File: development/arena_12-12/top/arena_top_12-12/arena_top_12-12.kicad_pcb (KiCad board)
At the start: 6 copper layers, 228.6 x 228.6 mm, 29 parts, among them J4 Barrel_Jack, P1 CONN15, P10 CONN15, P11 CONN15, P12 CONN15, P2 CONN15, P3 CONN15, P4 CONN15, P5 CONN15, P6 CONN15, P7 CONN15, P8 CONN15, P9 CONN15

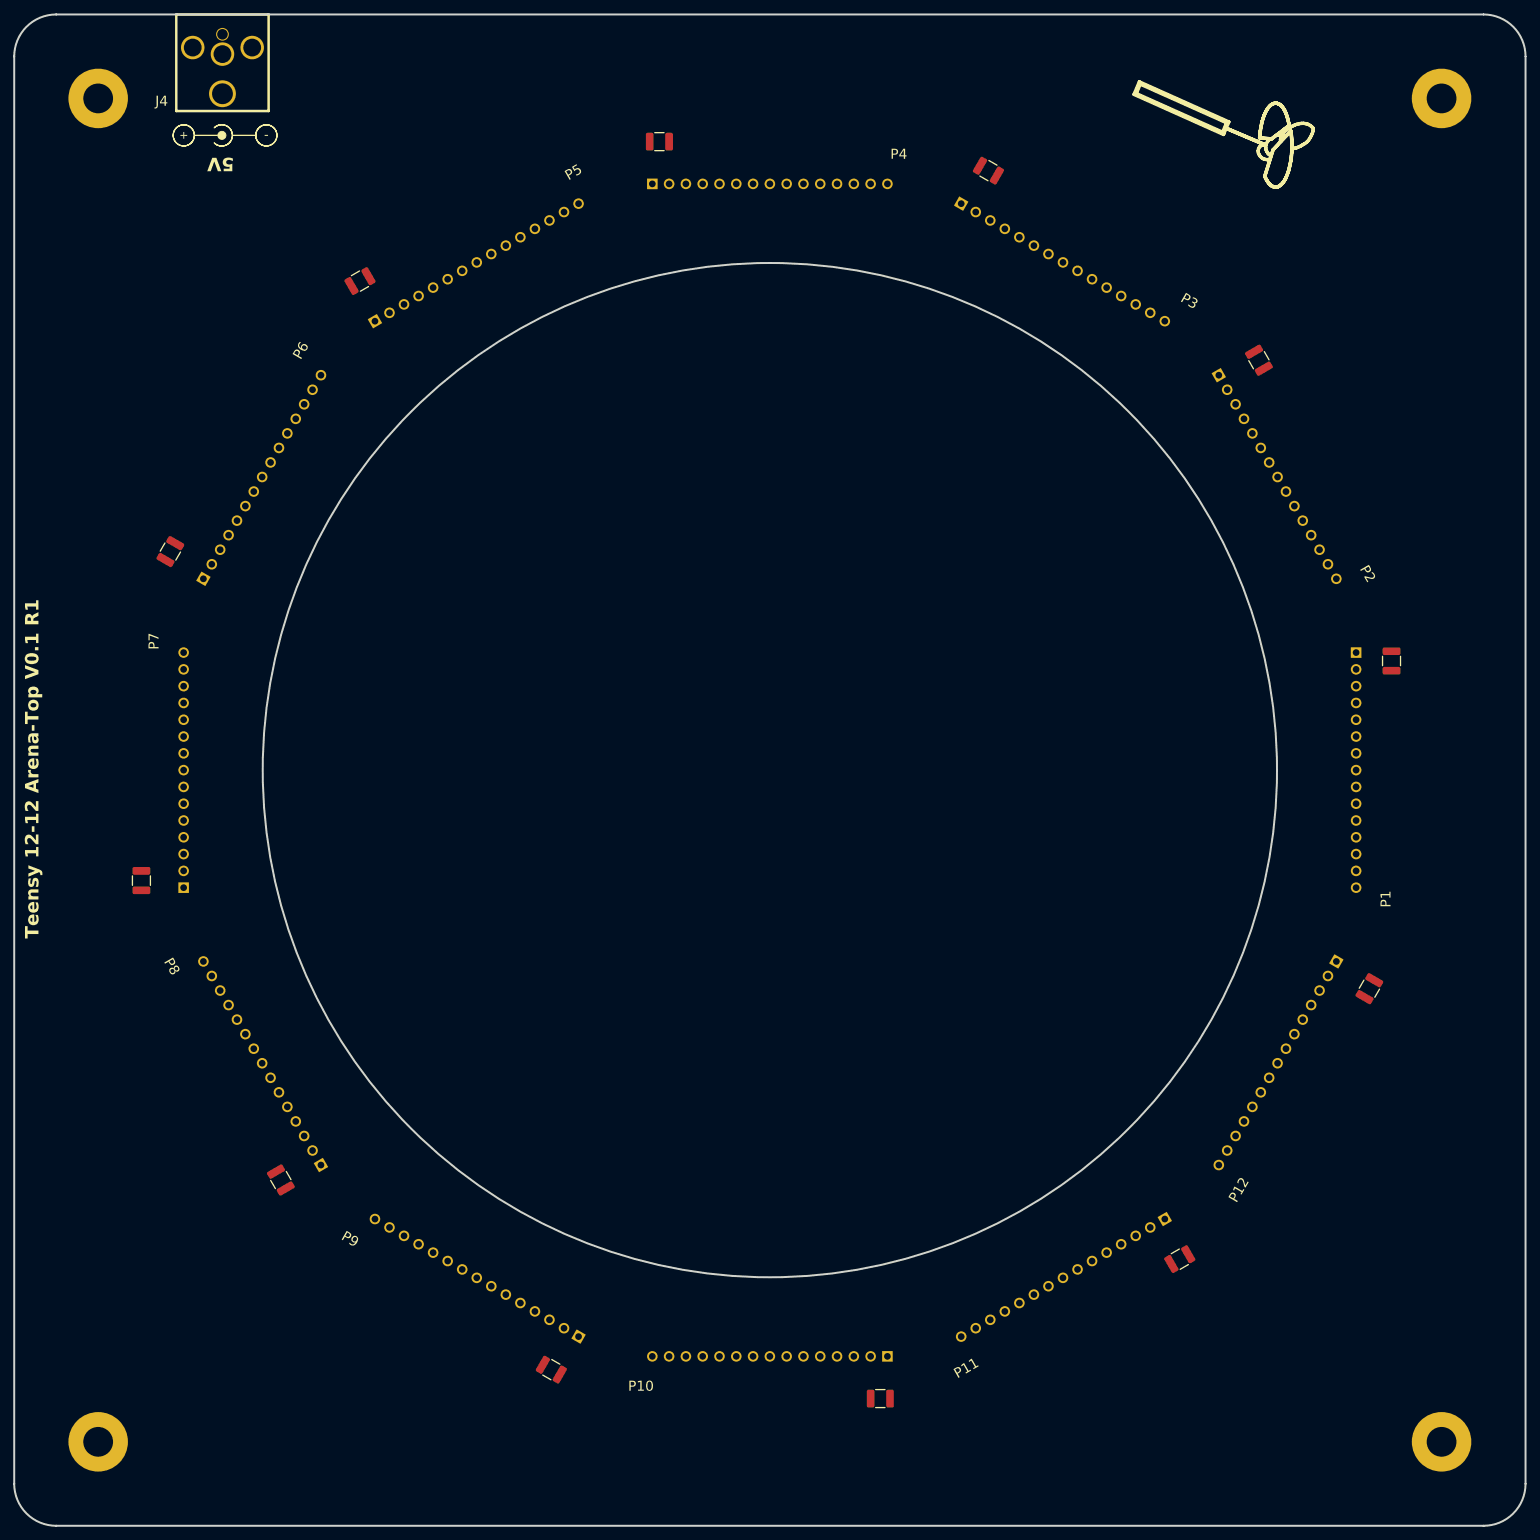
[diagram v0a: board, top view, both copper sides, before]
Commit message: Finished hand route of 12-12 teensy arena. Finished route of 12-12 top.
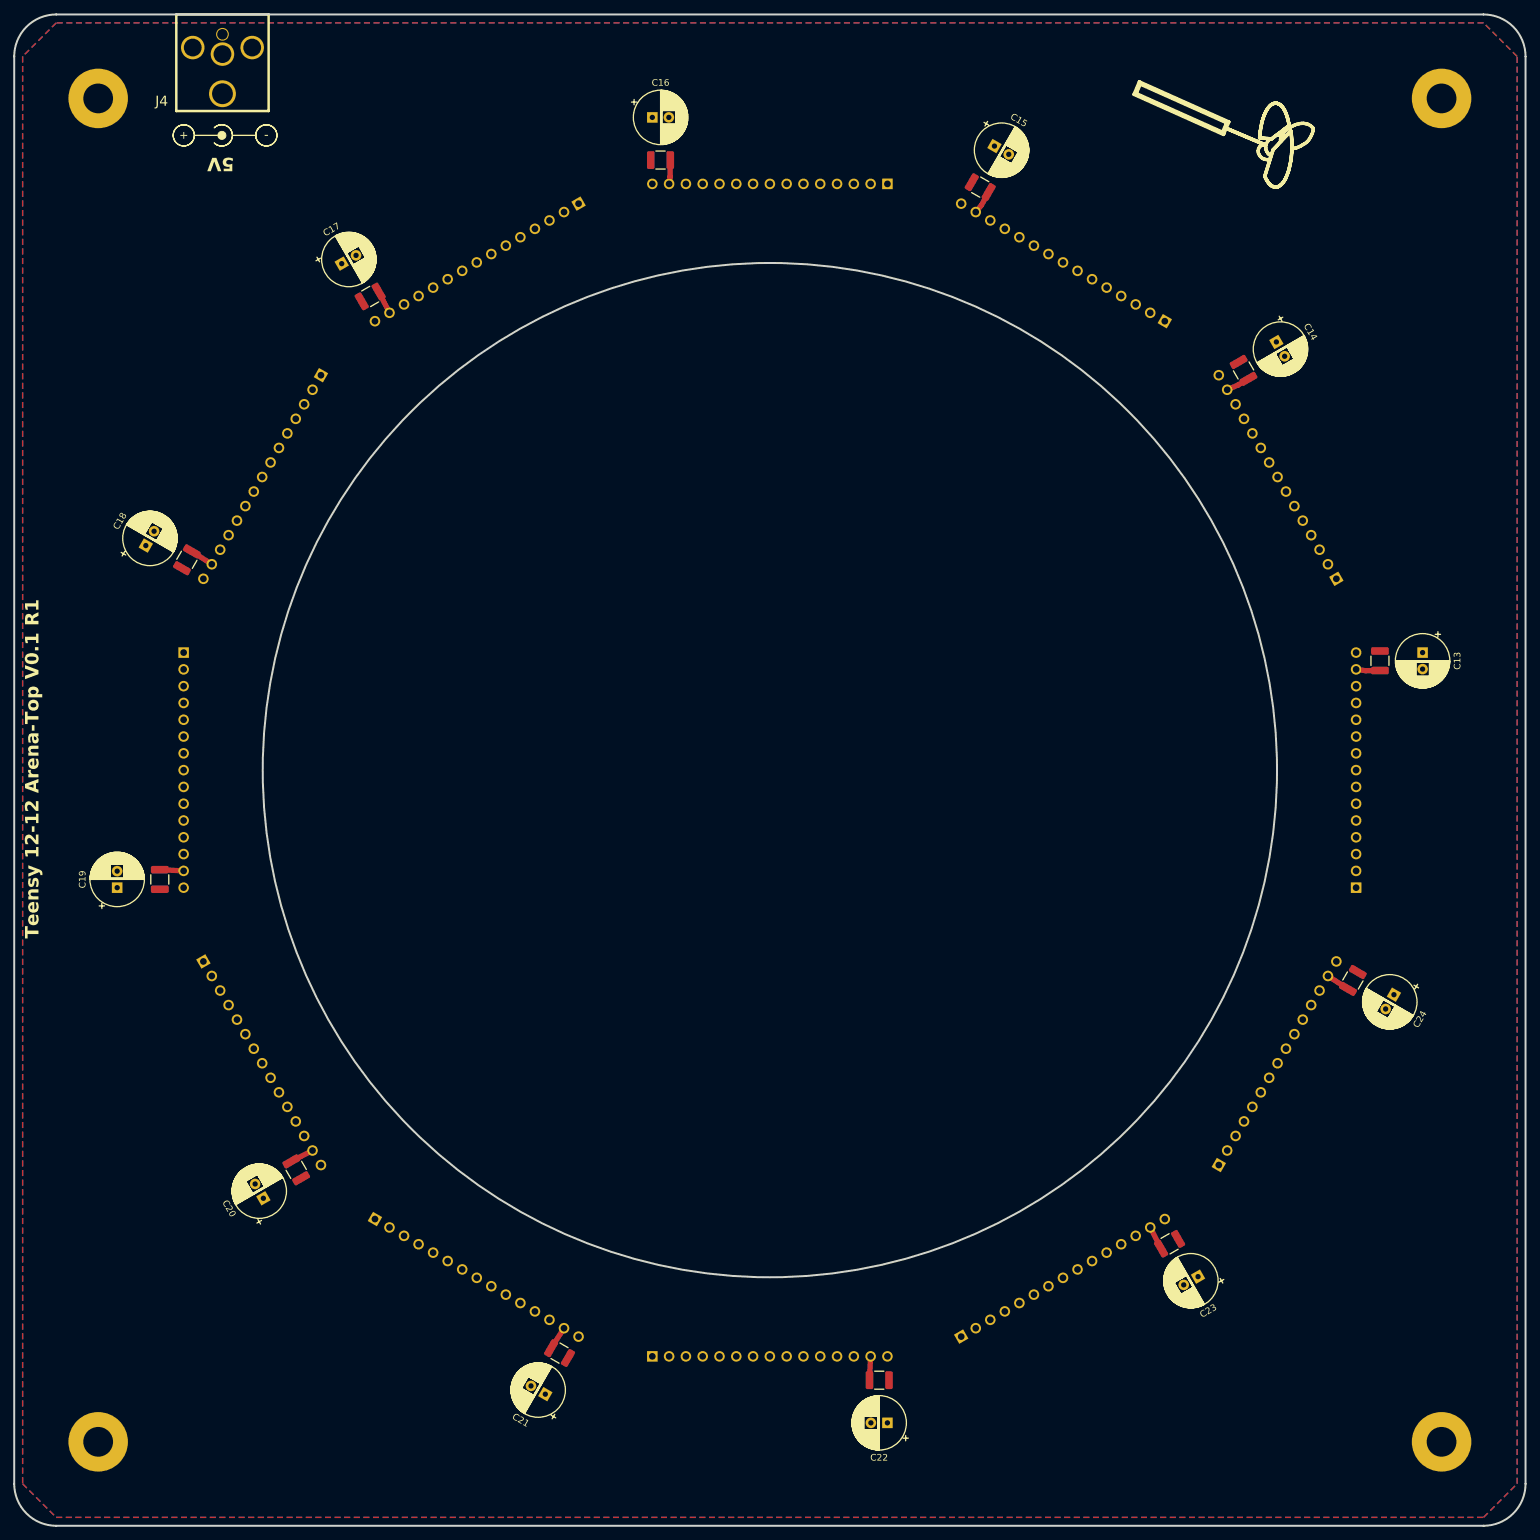
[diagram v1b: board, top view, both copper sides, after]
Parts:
- added C13: C_Polarized, Capacitor_THT:CP_Radial_D8.0mm_P2.50mm, F.Cu at (276.5, 160.0)
- added C14: C_Polarized, Capacitor_THT:CP_Radial_D8.0mm_P2.50mm, F.Cu at (254.4, 113.0)
- added C15: C_Polarized, Capacitor_THT:CP_Radial_D8.0mm_P2.50mm, F.Cu at (211.8, 83.4)
- added C16: C_Polarized, Capacitor_THT:CP_Radial_D8.0mm_P2.50mm, F.Cu at (160.0, 79.1)
- added C17: C_Polarized, Capacitor_THT:CP_Radial_D8.0mm_P2.50mm, F.Cu at (113.0, 101.2)
- added C18: C_Polarized, Capacitor_THT:CP_Radial_D8.0mm_P2.50mm, F.Cu at (83.4, 143.8)
- added C19: C_Polarized, Capacitor_THT:CP_Radial_D8.0mm_P2.50mm, F.Cu at (79.1, 195.6)
- added C20: C_Polarized, Capacitor_THT:CP_Radial_D8.0mm_P2.50mm, F.Cu at (101.2, 242.6)
- added C21: C_Polarized, Capacitor_THT:CP_Radial_D8.0mm_P2.50mm, F.Cu at (143.8, 272.2)
- added C22: C_Polarized, Capacitor_THT:CP_Radial_D8.0mm_P2.50mm, F.Cu at (195.6, 276.5)
- added C23: C_Polarized, Capacitor_THT:CP_Radial_D8.0mm_P2.50mm, F.Cu at (242.6, 254.4)
- added C24: C_Polarized, Capacitor_THT:CP_Radial_D8.0mm_P2.50mm, F.Cu at (272.2, 211.8)
- P1, P10, P11, P12, P2, P3, P4, P5, P6, P7, P8, P9: moved to B.Cu
- moved C10 2.79 mm to (194.3, 270.1)
- moved C4 2.79 mm to (161.3, 85.5)
- moved C7 2.79 mm to (85.5, 194.3)
- moved C2 2.79 mm to (249.4, 117.3)
- moved C5 2.79 mm to (117.3, 106.2)
- moved C11 2.79 mm to (238.3, 249.4)
- moved C8 2.79 mm to (106.2, 238.3)
- moved C12 2.79 mm to (266.0, 209.6)
- moved C9 2.79 mm to (146.0, 266.0)
- moved C3 2.79 mm to (209.6, 89.6)
- moved C6 2.79 mm to (89.6, 146.0)
- moved C1 1.75 mm to (270.1, 161.3)
- turned P1 to 90 degrees
- turned P10 to 0 degrees
- turned P11 to 30 degrees
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- renumbered C95 to C1, C104 to C10, C105 to C11, C106 to C12, C96 to C2, C97 to C3, C98 to C4, C99 to C5, C100 to C6, C101 to C7, C102 to C8, C103 to C9
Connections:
- P1 pad 1: +5V -> unconnected-(P1-Pad1)
- P1 pad 10: /Panel Headers/HDR_CS_03_P1 -> unconnected-(P1-Pad10)
- P1 pad 11: /Panel Headers/HDR_CS_04_P1 -> unconnected-(P1-Pad11)
- P1 pad 14: unconnected-(P1-Pad14) -> GND
- P1 pad 15: /Panel Headers/HDR_EXT_INT_P1 -> +5V
- P1 pad 2: GND -> unconnected-(P1-Pad2)
- P1 pad 3: /Panel Headers/HDR_RESET -> unconnected-(P1-Pad3)
- P1 pad 4: /Panel Headers/HDR_SCK_0_P1 -> unconnected-(P1-Pad4)
- P1 pad 5: /Panel Headers/HDR_MOSI_0_P1 -> unconnected-(P1-Pad5)
- P1 pad 6: /Panel Headers/HDR_MISO_0_P1 -> unconnected-(P1-Pad6)
- P1 pad 7: /Panel Headers/HDR_CS_00_P1 -> unconnected-(P1-Pad7)
- P1 pad 8: /Panel Headers/HDR_CS_01_P1 -> unconnected-(P1-Pad8)
- P1 pad 9: /Panel Headers/HDR_CS_02_P1 -> unconnected-(P1-Pad9)
- P10 pad 1: +5V -> unconnected-(P10-Pad1)
- P10 pad 10: /Panel Headers/HDR_CS_18_P10 -> unconnected-(P10-Pad10)
- P10 pad 11: /Panel Headers/HDR_CS_19_P10 -> unconnected-(P10-Pad11)
- P10 pad 14: unconnected-(P10-Pad14) -> GND
- P10 pad 15: /Panel Headers/HDR_EXT_INT_P10 -> +5V
- P10 pad 2: GND -> unconnected-(P10-Pad2)
- P10 pad 3: /Panel Headers/HDR_RESET -> unconnected-(P10-Pad3)
- P10 pad 4: /Panel Headers/HDR_SCK_1_P10 -> unconnected-(P10-Pad4)
- P10 pad 5: /Panel Headers/HDR_MOSI_1_P10 -> unconnected-(P10-Pad5)
- P10 pad 6: /Panel Headers/HDR_MISO_1_P10 -> unconnected-(P10-Pad6)
- P10 pad 7: /Panel Headers/HDR_CS_15_P10 -> unconnected-(P10-Pad7)
- P10 pad 8: /Panel Headers/HDR_CS_16_P10 -> unconnected-(P10-Pad8)
- P10 pad 9: /Panel Headers/HDR_CS_17_P10 -> unconnected-(P10-Pad9)
- P11 pad 1: +5V -> unconnected-(P11-Pad1)
- P11 pad 10: /Panel Headers/HDR_CS_23_P11 -> unconnected-(P11-Pad10)
- P11 pad 11: /Panel Headers/HDR_CS_24_P11 -> unconnected-(P11-Pad11)
- P11 pad 14: unconnected-(P11-Pad14) -> GND
- P11 pad 15: /Panel Headers/HDR_EXT_INT_P11 -> +5V
- P11 pad 2: GND -> unconnected-(P11-Pad2)
- P11 pad 3: /Panel Headers/HDR_RESET -> unconnected-(P11-Pad3)
- P11 pad 4: /Panel Headers/HDR_SCK_1_P11 -> unconnected-(P11-Pad4)
- P11 pad 5: /Panel Headers/HDR_MOSI_1_P11 -> unconnected-(P11-Pad5)
- P11 pad 6: /Panel Headers/HDR_MISO_1_P11 -> unconnected-(P11-Pad6)
- P11 pad 7: /Panel Headers/HDR_CS_20_P11 -> unconnected-(P11-Pad7)
- P11 pad 8: /Panel Headers/HDR_CS_21_P11 -> unconnected-(P11-Pad8)
- P11 pad 9: /Panel Headers/HDR_CS_22_P11 -> unconnected-(P11-Pad9)
- P12 pad 1: +5V -> unconnected-(P12-Pad1)
- P12 pad 10: /Panel Headers/HDR_CS_28_P12 -> unconnected-(P12-Pad10)
- P12 pad 11: /Panel Headers/HDR_CS_29_P12 -> unconnected-(P12-Pad11)
- P12 pad 14: unconnected-(P12-Pad14) -> GND
- P12 pad 15: /Panel Headers/HDR_EXT_INT_P12 -> +5V
- P12 pad 2: GND -> unconnected-(P12-Pad2)
- P12 pad 3: /Panel Headers/HDR_RESET -> unconnected-(P12-Pad3)
- P12 pad 4: /Panel Headers/HDR_SCK_1_P12 -> unconnected-(P12-Pad4)
- P12 pad 5: /Panel Headers/HDR_MOSI_1_P12 -> unconnected-(P12-Pad5)
- P12 pad 6: /Panel Headers/HDR_MISO_1_P12 -> unconnected-(P12-Pad6)
- P12 pad 7: /Panel Headers/HDR_CS_25_P12 -> unconnected-(P12-Pad7)
- P12 pad 8: /Panel Headers/HDR_CS_26_P12 -> unconnected-(P12-Pad8)
- P12 pad 9: /Panel Headers/HDR_CS_27_P12 -> unconnected-(P12-Pad9)
- P2 pad 1: +5V -> unconnected-(P2-Pad1)
- P2 pad 10: /Panel Headers/HDR_CS_08_P2 -> unconnected-(P2-Pad10)
- P2 pad 11: /Panel Headers/HDR_CS_09_P2 -> unconnected-(P2-Pad11)
- P2 pad 14: unconnected-(P2-Pad14) -> GND
- P2 pad 15: /Panel Headers/HDR_EXT_INT_P2 -> +5V
- P2 pad 2: GND -> unconnected-(P2-Pad2)
- P2 pad 3: /Panel Headers/HDR_RESET -> unconnected-(P2-Pad3)
- P2 pad 4: /Panel Headers/HDR_SCK_0_P2 -> unconnected-(P2-Pad4)
- P2 pad 5: /Panel Headers/HDR_MOSI_0_P2 -> unconnected-(P2-Pad5)
- P2 pad 6: /Panel Headers/HDR_MISO_0_P2 -> unconnected-(P2-Pad6)
- P2 pad 7: /Panel Headers/HDR_CS_05_P2 -> unconnected-(P2-Pad7)
- P2 pad 8: /Panel Headers/HDR_CS_06_P2 -> unconnected-(P2-Pad8)
- P2 pad 9: /Panel Headers/HDR_CS_07_P2 -> unconnected-(P2-Pad9)
- P3 pad 1: +5V -> unconnected-(P3-Pad1)
- P3 pad 10: /Panel Headers/HDR_CS_13_P3 -> unconnected-(P3-Pad10)
- P3 pad 11: /Panel Headers/HDR_CS_14_P3 -> unconnected-(P3-Pad11)
- P3 pad 14: unconnected-(P3-Pad14) -> GND
- P3 pad 15: /Panel Headers/HDR_EXT_INT_P3 -> +5V
- P3 pad 2: GND -> unconnected-(P3-Pad2)
- P3 pad 3: /Panel Headers/HDR_RESET -> unconnected-(P3-Pad3)
- P3 pad 4: /Panel Headers/HDR_SCK_0_P3 -> unconnected-(P3-Pad4)
- P3 pad 5: /Panel Headers/HDR_MOSI_0_P3 -> unconnected-(P3-Pad5)
- P3 pad 6: /Panel Headers/HDR_MISO_0_P3 -> unconnected-(P3-Pad6)
- P3 pad 7: /Panel Headers/HDR_CS_10_P3 -> unconnected-(P3-Pad7)
- P3 pad 8: /Panel Headers/HDR_CS_11_P3 -> unconnected-(P3-Pad8)
- P3 pad 9: /Panel Headers/HDR_CS_12_P3 -> unconnected-(P3-Pad9)
- P4 pad 1: +5V -> unconnected-(P4-Pad1)
- P4 pad 10: /Panel Headers/HDR_CS_18_P4 -> unconnected-(P4-Pad10)
- P4 pad 11: /Panel Headers/HDR_CS_19_P4 -> unconnected-(P4-Pad11)
- P4 pad 14: unconnected-(P4-Pad14) -> GND
- P4 pad 15: /Panel Headers/HDR_EXT_INT_P4 -> +5V
- P4 pad 2: GND -> unconnected-(P4-Pad2)
- P4 pad 3: /Panel Headers/HDR_RESET -> unconnected-(P4-Pad3)
- P4 pad 4: /Panel Headers/HDR_SCK_0_P4 -> unconnected-(P4-Pad4)
- P4 pad 5: /Panel Headers/HDR_MOSI_0_P4 -> unconnected-(P4-Pad5)
- P4 pad 6: /Panel Headers/HDR_MISO_0_P4 -> unconnected-(P4-Pad6)
- P4 pad 7: /Panel Headers/HDR_CS_15_P4 -> unconnected-(P4-Pad7)
- P4 pad 8: /Panel Headers/HDR_CS_16_P4 -> unconnected-(P4-Pad8)
- P4 pad 9: /Panel Headers/HDR_CS_17_P4 -> unconnected-(P4-Pad9)
- P5 pad 1: +5V -> unconnected-(P5-Pad1)
- P5 pad 10: /Panel Headers/HDR_CS_23_P5 -> unconnected-(P5-Pad10)
- P5 pad 11: /Panel Headers/HDR_CS_24_P5 -> unconnected-(P5-Pad11)
- P5 pad 14: unconnected-(P5-Pad14) -> GND
- P5 pad 15: /Panel Headers/HDR_EXT_INT_P5 -> +5V
- P5 pad 2: GND -> unconnected-(P5-Pad2)
- P5 pad 3: /Panel Headers/HDR_RESET -> unconnected-(P5-Pad3)
- P5 pad 4: /Panel Headers/HDR_SCK_0_P5 -> unconnected-(P5-Pad4)
- P5 pad 5: /Panel Headers/HDR_MOSI_0_P5 -> unconnected-(P5-Pad5)
- P5 pad 6: /Panel Headers/HDR_MISO_0_P5 -> unconnected-(P5-Pad6)
- P5 pad 7: /Panel Headers/HDR_CS_20_P5 -> unconnected-(P5-Pad7)
- P5 pad 8: /Panel Headers/HDR_CS_21_P5 -> unconnected-(P5-Pad8)
- P5 pad 9: /Panel Headers/HDR_CS_22_P5 -> unconnected-(P5-Pad9)
- P6 pad 1: +5V -> unconnected-(P6-Pad1)
- P6 pad 10: /Panel Headers/HDR_CS_28_P6 -> unconnected-(P6-Pad10)
- P6 pad 11: /Panel Headers/HDR_CS_29_P6 -> unconnected-(P6-Pad11)
- P6 pad 14: unconnected-(P6-Pad14) -> GND
- P6 pad 15: /Panel Headers/HDR_EXT_INT_P6 -> +5V
- P6 pad 2: GND -> unconnected-(P6-Pad2)
- P6 pad 3: /Panel Headers/HDR_RESET -> unconnected-(P6-Pad3)
- P6 pad 4: /Panel Headers/HDR_SCK_0_P6 -> unconnected-(P6-Pad4)
- P6 pad 5: /Panel Headers/HDR_MOSI_0_P6 -> unconnected-(P6-Pad5)
- P6 pad 6: /Panel Headers/HDR_MISO_0_P6 -> unconnected-(P6-Pad6)
- P6 pad 7: /Panel Headers/HDR_CS_25_P6 -> unconnected-(P6-Pad7)
- P6 pad 8: /Panel Headers/HDR_CS_26_P6 -> unconnected-(P6-Pad8)
- P6 pad 9: /Panel Headers/HDR_CS_27_P6 -> unconnected-(P6-Pad9)
- P7 pad 1: +5V -> unconnected-(P7-Pad1)
- P7 pad 10: /Panel Headers/HDR_CS_03_P7 -> unconnected-(P7-Pad10)
- P7 pad 11: /Panel Headers/HDR_CS_04_P7 -> unconnected-(P7-Pad11)
- P7 pad 14: unconnected-(P7-Pad14) -> GND
- P7 pad 15: /Panel Headers/HDR_EXT_INT_P7 -> +5V
- P7 pad 2: GND -> unconnected-(P7-Pad2)
- P7 pad 3: /Panel Headers/HDR_RESET -> unconnected-(P7-Pad3)
- P7 pad 4: /Panel Headers/HDR_SCK_1_P7 -> unconnected-(P7-Pad4)
- P7 pad 5: /Panel Headers/HDR_MOSI_1_P7 -> unconnected-(P7-Pad5)
- P7 pad 6: /Panel Headers/HDR_MISO_1_P7 -> unconnected-(P7-Pad6)
- P7 pad 7: /Panel Headers/HDR_CS_00_P7 -> unconnected-(P7-Pad7)
- P7 pad 8: /Panel Headers/HDR_CS_01_P7 -> unconnected-(P7-Pad8)
- P7 pad 9: /Panel Headers/HDR_CS_02_P7 -> unconnected-(P7-Pad9)
- P8 pad 1: +5V -> unconnected-(P8-Pad1)
- P8 pad 10: /Panel Headers/HDR_CS_08_P8 -> unconnected-(P8-Pad10)
- P8 pad 11: /Panel Headers/HDR_CS_09_P8 -> unconnected-(P8-Pad11)
- P8 pad 14: unconnected-(P8-Pad14) -> GND
- P8 pad 15: /Panel Headers/HDR_EXT_INT_P8 -> +5V
- P8 pad 2: GND -> unconnected-(P8-Pad2)
- P8 pad 3: /Panel Headers/HDR_RESET -> unconnected-(P8-Pad3)
- P8 pad 4: /Panel Headers/HDR_SCK_1_P8 -> unconnected-(P8-Pad4)
- P8 pad 5: /Panel Headers/HDR_MOSI_1_P8 -> unconnected-(P8-Pad5)
- P8 pad 6: /Panel Headers/HDR_MISO_1_P8 -> unconnected-(P8-Pad6)
- P8 pad 7: /Panel Headers/HDR_CS_05_P8 -> unconnected-(P8-Pad7)
- P8 pad 8: /Panel Headers/HDR_CS_06_P8 -> unconnected-(P8-Pad8)
- P8 pad 9: /Panel Headers/HDR_CS_07_P8 -> unconnected-(P8-Pad9)
- P9 pad 1: +5V -> unconnected-(P9-Pad1)
- P9 pad 10: /Panel Headers/HDR_CS_13_P9 -> unconnected-(P9-Pad10)
- P9 pad 11: /Panel Headers/HDR_CS_14_P9 -> unconnected-(P9-Pad11)
- P9 pad 14: unconnected-(P9-Pad14) -> GND
- P9 pad 15: /Panel Headers/HDR_EXT_INT_P9 -> +5V
- P9 pad 2: GND -> unconnected-(P9-Pad2)
- P9 pad 3: /Panel Headers/HDR_RESET -> unconnected-(P9-Pad3)
- P9 pad 4: /Panel Headers/HDR_SCK_1_P9 -> unconnected-(P9-Pad4)
- P9 pad 5: /Panel Headers/HDR_MOSI_1_P9 -> unconnected-(P9-Pad5)
- P9 pad 6: /Panel Headers/HDR_MISO_1_P9 -> unconnected-(P9-Pad6)
- P9 pad 7: /Panel Headers/HDR_CS_10_P9 -> unconnected-(P9-Pad7)
- P9 pad 8: /Panel Headers/HDR_CS_11_P9 -> unconnected-(P9-Pad8)
- P9 pad 9: /Panel Headers/HDR_CS_12_P9 -> unconnected-(P9-Pad9)
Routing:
- net GND: track 0.00 -> 43.3 mm
- added copper zone on F.Cu, net +5V
- added copper zone on B.Cu, net GND
- removed copper zone on In2.Cu, net +5V
- removed copper zone on In1.Cu, net GND
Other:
- copper layers 6 -> 2
